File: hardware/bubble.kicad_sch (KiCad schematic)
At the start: 56 parts, among them J1 Barrel_Jack_Switch, Q1 AO3400A, U1 i7220, U2 i7230, U3 i7254, U4 i7250, U5 i7254, U6 i7242, U7 LM7805_TO220

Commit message: hardware: new board schematic
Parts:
- removed A1: Arduino_Nano_v3.x, Module:Arduino_Nano, symbol MCU_Module:Arduino_Nano_v3.x
- removed C1, C11, C13, C15, C16, C17, C2, C21, C3, C9: 100nF, Capacitor_SMD:C_0603_1608Metric, symbol Device:C_Small
- removed C10, C12, C14, C18, C22, C4, C5, C6, C7, C8: 22uF, Capacitor_SMD:C_1206_3216Metric, symbol Device:C_Small
- removed C19, C20: 120pF, Capacitor_SMD:C_0603_1608Metric, symbol Device:C_Small
- removed C23: 1uF, Capacitor_SMD:C_0603_1608Metric, symbol Device:C_Small
- removed C24: 2.2uF, Capacitor_SMD:C_0603_1608Metric, symbol Device:C_Small
- removed C25, C26: 1000uF, Capacitor_THT:CP_Radial_D8.0mm_P5.00mm, symbol Device:C_Polarized_Small_US
- removed J1: Barrel_Jack_Switch, Connector_BarrelJack:BarrelJack_GCT_DCJ200-10-A_Horizontal, symbol Connector:Barrel_Jack_Switch
- removed JP1, JP2: ~, Connector_PinSocket_2.54mm:PinSocket_1x02_P2.54mm_Vertical, symbol Jumper:Jumper_2_Bridged
- removed L1, L2, L3: .22uH, Inductor_SMD:L_1008_2520Metric, symbol Device:L_Small
- removed Q1: AO3400A, Package_TO_SOT_SMD:SOT-23, symbol Transistor_FET:AO3400A
- removed R1, R3, R5: 5.6k, Resistor_SMD:R_0603_1608Metric, symbol Device:R_Small
- removed R10, R11, R8, R9: 1k 2W, Resistor_SMD:R_2512_6332Metric, symbol Device:R_Small
- removed R12, R6: 5.1, Resistor_SMD:R_0805_2012Metric, symbol Device:R_Small
- removed R13: 33k, Resistor_SMD:R_0603_1608Metric, symbol Device:R_Small
- removed R14: 12k, Resistor_SMD:R_0603_1608Metric, symbol Device:R_Small
- removed R2: 3.48k 1%, Resistor_SMD:R_0603_1608Metric, symbol Device:R_Small
- removed R4: 47, Resistor_SMD:R_0805_2012Metric, symbol Device:R_Small
- removed R7: 10, Resistor_SMD:R_0603_1608Metric, symbol Device:R_Small
- removed U1: i7220, Package_DIP:DIP-40_W15.24mm, symbol intel_bubble:i7220
- removed U2: i7230, Package_DIP:DIP-22_W7.62mm, symbol intel_bubble:i7230
- removed U3, U5: i7254, Package_DIP:DIP-14_W7.62mm, symbol intel_bubble:i7254
- removed U4: i7250, Package_DIP:DIP-16_W7.62mm, symbol intel_bubble:i7250
- removed U6: i7242, Package_DIP:DIP-20_W7.62mm, symbol intel_bubble:i7242
- removed U7: LM7805_TO220, Package_TO_SOT_THT:TO-220-3_Vertical, symbol Regulator_Linear:LM7805_TO220
- added C1, C4: 0.33 uF, symbol Device:C
- added C10, C15: 15uF 20V 20%, symbol Device:C
- added C11, C12: 120pF 100V 5%, symbol Device:C
- added C13, C14, C8: 0.1uF, symbol Device:C
- added C2: 47 uF, symbol Device:C
- added C3, C5: 0.1 uF, symbol Device:C
- added C6: 120 uF, symbol Device:C
- added C7: 2.2 uF 20V 10%, symbol Device:C
- added C9: 15uF 20V 20%, symbol Device:C_Polarized
- added JP1: Only for reseed, Connector_PinHeader_2.54mm:PinHeader_1x02_P2.54mm_Vertical, symbol Jumper:Jumper_2_Open
- added L1, L2, L3: 0.22 uH, Inductor_SMD:L_0603_1608Metric_Pad1.05x0.95mm_HandSolder, symbol Device:L
- added Q1: BS170, Package_TO_SOT_THT:TO-92_Inline, symbol Transistor_FET:BS170
- added R1, R3: 33 kOhm, Resistor_SMD:R_0805_2012Metric_Pad1.20x1.40mm_HandSolder, symbol Device:R
- added R10, R11, R8, R9: 1kOhm, Resistor_SMD:R_0805_2012Metric_Pad1.20x1.40mm_HandSolder, symbol Device:R
- added R12, R7: 5.1 kOhm, Resistor_SMD:R_0805_2012Metric_Pad1.20x1.40mm_HandSolder, symbol Device:R
- added R13: 10Ohm, Resistor_SMD:R_0805_2012Metric_Pad1.20x1.40mm_HandSolder, symbol Device:R
- added R2: 3.48 kOhm, Resistor_SMD:R_0805_2012Metric_Pad1.20x1.40mm_HandSolder, symbol Device:R
- added R4, R5: 5.1 Ohm, Resistor_SMD:R_0805_2012Metric_Pad1.20x1.40mm_HandSolder, symbol Device:R
- added R6: 47 Ohm, Resistor_SMD:R_0805_2012Metric_Pad1.20x1.40mm_HandSolder, symbol Device:R
- added U1, U4: i7254, Package_DIP:DIP-14_W7.62mm, symbol intel_bubble:i7254
- added U2: i7250, Package_DIP:DIP-16_W7.62mm, symbol intel_bubble:i7250
- added U3: 74LS74, Package_DIP:DIP-14_W7.62mm, symbol 74xx:74LS74
- added U5: i7230, Package_DIP:DIP-22_W10.16mm, symbol intel_bubble:i7230
- added U6: i7220, Package_DIP:DIP-40_W15.24mm, symbol intel_bubble:i7220
- added U7: i7242, Package_DIP:DIP-20_W7.62mm, symbol intel_bubble:i7242
- added Y1: 8.000 MHz, Oscillator:Oscillator_DIP-8, symbol Oscillator:CXO_DIP8
- MBM1: footprint intel_bubble:MBM_dual -> intel_bubble:MBM_socket; LCSC Part # N/A -> (none)
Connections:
- net SWAP is gone; now on an unnamed net: MBM1.14 (SWAP.B)
- net +12V: now also JP1.2 (B), L1.1, R13.2, R4.2, R6.2, U1.13 (S4), U1.6 (S2), U4.13 (S4), U4.6 (S2)
- net +5V: now also C13.1, L2.1, R12.1, R3.2, R7.1, U3.1 (~{R}), U3.14 (VCC), U3.4 (~{S}), U7.20 (VCC), Y1.1 (EN), Y1.8 (Vcc)
- net A0: now also U6.10 (A0)
- net CLK: now also U3.5 (Q), U6.3 (CLK), U7.18 (CLK)
- net D0: now also U6.11 (D0)
- net D1: now also U6.12 (D1)
- net D2: now also U6.13 (D2)
- net D3: now also U6.14 (D3)
- net D4: now also U6.15 (D4)
- net D5: now also U6.16 (D5)
- net D6: now also U6.17 (D6)
- net D7: now also U6.18 (D7)
- net GND: now also C1.2, C13.2, C14.2, C15.2, C2.2, C3.2, C4.2, C5.2, C6.2, C7.1, Q1.3 (S), R5.1, U1.2 (S1), U1.9 (S3), U2.8 (GND), U3.7 (GND), U4.2 (S1), U4.9 (S3), U5.11 (GND), U5.12 (GND), U6.20 (GND), U7.1 (~{CS}), U7.10 (GND), Y1.4 (GND)
- net INT: now also U6.9 (INT)
- net ~{BUS.RD}: now also U6.25 (~{BUS.RD})
- net ~{DACK}: now also U6.7 (~{DACK})
- net ~{RD}: now also U6.5 (~{RD})
- net ~{WAIT}: now also R12.2, U6.26 (~{WAIT})
- net ~{WR}: now also U6.6 (~{WR})
- net at MBM1.1 (PULSE.COM(+12V)), MBM1.6 (PULSE.COM(+12V)): now also C10.2
- net at MBM1.17 (DET.OUT.B+): now also R9.1
- net at MBM1.18 (DET.OUT.A-): now also R10.1
- net at MBM1.20 (DET.SUPPLY): now also C8.1, C9.1, R4.1
- net at MBM1.15 (DET.COM): now also C8.2, C9.2, R5.2
- net at MBM1.13 (SWAP.A): now also U5.17 (SWAP)
- net at MBM1.16 (DET.OUT.B-): now also R8.1
- net at MBM1.19 (DET.OUT.A+): now also R11.1
- net BOOT.REP: no longer names the net of MBM1.4 (BOOT.REP)
- net BOOT.REP: now also U5.13 (BOOT.REP)
- net BOOT.SWAP: no longer names the net of MBM1.5 (BOOT.SWAP)
- net BOOT.SWAP: now also U5.14 (BOOT.SWAP)
- net GEN.A: no longer names the net of MBM1.7 (GEN.A)
- net GEN.A: now also U5.18 (GEN.A)
- net GEN.B: no longer names the net of MBM1.8 (GEN.B)
- net GEN.B: now also U5.19 (GEN.B)
- net REP.A: no longer names the net of MBM1.3 (REP.A)
- net REP.A: now also U5.15 (REP.A)
- net REP.B: no longer names the net of MBM1.2 (REP.B)
- net REP.B: now also U5.16 (REP.B)
- net X+.COIL: no longer names the net of MBM1.10 (X+.COIL.IN)
- net X+.COIL: now also U1.1 (D1), U1.14 (D4)
- net X-.COIL: no longer names the net of MBM1.9 (X-.COIL.IN)
- net X-.COIL: now also U1.7 (D2), U1.8 (D3)
- net Y+.COIL: no longer names the net of MBM1.12 (Y+.COIL.IN)
- net Y+.COIL: now also U4.1 (D1), U4.14 (D4)
- net Y-.COIL: no longer names the net of MBM1.11 (Y-.COIL.IN)
- net Y-.COIL: now also U4.7 (D2), U4.8 (D3)
- new net: C7.2, R1.1, R3.1, U5.21 (~{PWR.FAIL}), U6.1 (~{PWR.FAIL})
- new net: C11.1, R11.2, U7.6 (DET.A+)
- new net: C11.2, R10.2, U7.7 (DET.A-)
- new net: C4.1, L2.2, L3.1
- new net: U3.3 (C), Y1.5 (OUT)
- new net: C14.1, C15.1, R13.1, U7.5 (VDD)
- new net: U3.2 (D), U3.6 (~{Q})
- new net: Q1.1 (D), R2.1
- new net: R2.2, U5.20 (REFR)
- new net: U2.1 (~{CS}), U5.7 (~{CS}), U7.13 (~{ENABLE.A})
- new net: U2.10 (Y+.OUT), U4.10 (G3)
- new net: U2.11 (~{Y+.OUT}), U4.12 (G4)
- new net: U1.3 (G1), U2.12 (X-.OUT)
- new net: U1.5 (G2), U2.13 (~{X-.OUT})
- new net: U1.10 (G3), U2.14 (X+.OUT)
- new net: U1.12 (G4), U2.15 (~{X+.OUT})
- new net: Q1.2 (G), R1.2, U2.2 (~{RESET}), U6.2 (~{RESET.OUT}), U7.16 (~{RESET})
- new net: U2.3 (~{X+.IN}), U6.39 (~{X+})
- new net: U2.4 (~{X-.IN}), U6.38 (~{X-})
- new net: U2.5 (~{Y+.IN}), U6.37 (~{Y+})
- new net: U2.6 (~{Y-.IN}), U6.36 (~{Y-})
- new net: U2.7 (Y-.OUT), U4.3 (G1)
- new net: U2.9 (~{Y-.OUT}), U4.5 (G2)
- new net: C10.1, JP1.1 (A), R6.1
- new net: C12.1, R9.2, U7.8 (DET.B+)
- new net: C12.2, R8.2, U7.9 (DET.B-)
- new net: U5.10 (~{BOOT.EN}), U6.32 (~{BOOT.EN})
- new net: U5.2 (~{TM.A}), U6.35 (~{TM.A})
- new net: U5.3 (~{TM.B}), U6.34 (~{TM.B})
- new net: U5.4 (~{GEN.EN.B}), U7.12 (~{DATA.OUT.B})
- new net: U5.5 (~{GEN.EN.A}), U7.11 (~{DATA.OUT.A})
- new net: U5.6 (~{SWAP.EN}), U6.31 (~{SWAP.EN})
- new net: U5.8 (~{REP.EN}), U6.33 (~{REP.EN})
- new net: U5.9 (~{BOOT.SW.EN}), U6.30 (~{BOOT.SW.EN})
- new net: U6.22 (DIO), U7.17 (DIO)
- new net: U6.23 (~{SYNC}), U7.19 (~{SELECT.IN})
- new net: U6.24 (~{SHIFT.CLK}), U7.15 (~{SHIFT.CLK})
- new net: U6.29 (C/~{D}), U7.3 (C/~{D})
- new net D8: U6.19 (D8)
- new net DRQ: U6.8 (DRQ)
- new net VCC_MBM_CH: C5.1, C6.1, L3.2, U5.22 (VCC), U6.40 (VCC)
- new net VDD_MBM_CH: C1.1, C2.1, C3.1, L1.2, U2.16 (VDD), U5.1 (VDD)
- new net ~{CS}: U6.21 (~{CS})
- new net ~{DET.ON}: U6.28 (~{DET.ON})
- new net ~{ERR_FLAG}: R7.2, U6.27 (~{ERR.FLG}), U7.4 (~{ERR.FLG})
- new net ~{RESET}: U6.4 (~{RESET})
- no-connect marks 21 -> 8
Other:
- note removed: "JUMPER PROVIDED FOR 7110AZ - SHORT FOR NON-AZ"
- company: UNIX-HATERS Federation -> (none)
- title: UHF Bubble Def*cker -> Bubblator

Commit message: hardware: add more capacitors, fix critical mistakes in schematic
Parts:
- removed C1, C4: 0.33 uF, symbol Device:C
- removed C2: 47 uF, symbol Device:C
- removed C3, C5: 0.1 uF, symbol Device:C
- removed C6: 120 uF, symbol Device:C
- removed L1, L2, L3: 0.22 uH, Inductor_SMD:L_0603_1608Metric_Pad1.05x0.95mm_HandSolder, symbol Device:L
- removed R10, R11, R8, R9: 1kOhm, Resistor_SMD:R_0805_2012Metric_Pad1.20x1.40mm_HandSolder, symbol Device:R
- added C24, C30, C31: 0.1uF, Capacitor_SMD:C_0805_2012Metric_Pad1.18x1.45mm_HandSolder, symbol Device:C
- added C28, C3, C32, C5, C6: 47uF, Capacitor_THT:CP_Radial_D5.0mm_P2.00mm, symbol Device:C_Polarized
- added C29, C33, C4: 22uF, Capacitor_THT:CP_Radial_D5.0mm_P2.00mm, symbol Device:C_Polarized
- added RN1: 1k, Resistor_THT:R_Array_SIP8, symbol Device:R_Pack04
- C10, C9: value 15uF 20V 20% -> 22uF 25V; footprint (none) -> Capacitor_THT:CP_Radial_D5.0mm_P2.00mm
- C11, C12: value 120pF 100V 5% -> 120 pF 100V 5%; footprint (none) -> Capacitor_THT:C_Disc_D5.0mm_W2.5mm_P2.50mm
- C13, C14, C8: footprint (none) -> Capacitor_SMD:C_0805_2012Metric_Pad1.18x1.45mm_HandSolder
- C15: value 15uF 20V 20% -> 0.1uF; footprint (none) -> Capacitor_SMD:C_0805_2012Metric_Pad1.18x1.45mm_HandSolder
- C7: value 2.2 uF 20V 10% -> 2.2uF; footprint (none) -> Capacitor_THT:C_Radial_D4.0mm_H7.0mm_P1.50mm
- R1, R3: value 33 kOhm -> 33k
- R12, R7: value 5.1 kOhm -> 5.1k
- R13: value 10Ohm -> 10
- R2: value 3.48 kOhm -> 3.48k
- R4, R5: value 5.1 Ohm -> 5.1
- R6: value 47 Ohm -> 47
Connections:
- net VCC_MBM_CH is gone; now on net +5V: U5.22 (VCC), U6.40 (VCC)
- net VDD_MBM_CH is gone; now on net +12V: U2.16 (VDD), U5.1 (VDD)
- net +12V: now also C28.1, C29.1, C30.1, C31.1, C32.1, C33.1
- net +5V: now also C15.1, C24.1, C3.1, C5.1, C6.1
- net GND: now also C24.2, C28.2, C29.2, C3.2, C30.2, C31.2, C32.2, C33.2, C4.2, C5.2, C6.2
- net at C11.1, U7.6 (DET.A+): now also RN1.4 (R4.1)
- net at C11.2, U7.7 (DET.A-): now also RN1.3 (R3.1)
- net at C14.1, R13.1, U7.5 (VDD): now also C4.1; no longer C15.1
- net at C12.1, U7.8 (DET.B+): now also RN1.2 (R2.1)
- net at C12.2, U7.9 (DET.B-): now also RN1.1 (R1.1)
- net at MBM1.18 (DET.OUT.A-): now also RN1.6 (R3.2)
- net at MBM1.19 (DET.OUT.A+): now also RN1.5 (R4.2)
- net at MBM1.16 (DET.OUT.B-): now also RN1.8 (R1.2)
- net at MBM1.17 (DET.OUT.B+): now also RN1.7 (R2.2)
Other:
- note added: "Clock generator"
- note added: "Pull-up resistors"
- moved on the sheet: C10, C11, C12, C13, C14, C7, C8, C9, JP1, MBM1, Q1, R1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

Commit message: hardware: minor cleanup
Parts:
- removed C7: 2.2uF, Capacitor_THT:C_Radial_D4.0mm_H7.0mm_P1.50mm, symbol Device:C
- added C34, C35: 2.2uF, Capacitor_THT:CP_Radial_D5.0mm_P2.00mm, symbol Device:C_Polarized
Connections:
- net GND: now also C34.2, C35.2
- net at R1.1, R3.1, U5.21 (~{PWR.FAIL})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: now also C34.1
- net at Q1.2 (G), R1.2, U2.2 (~{RESET})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: now also C35.1
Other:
- note added: "TODO: Verify this with Compass"
- moved on the sheet: C10, C11, C12, C13, C14, C15, C24, C28, C29, C3, C30, C31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

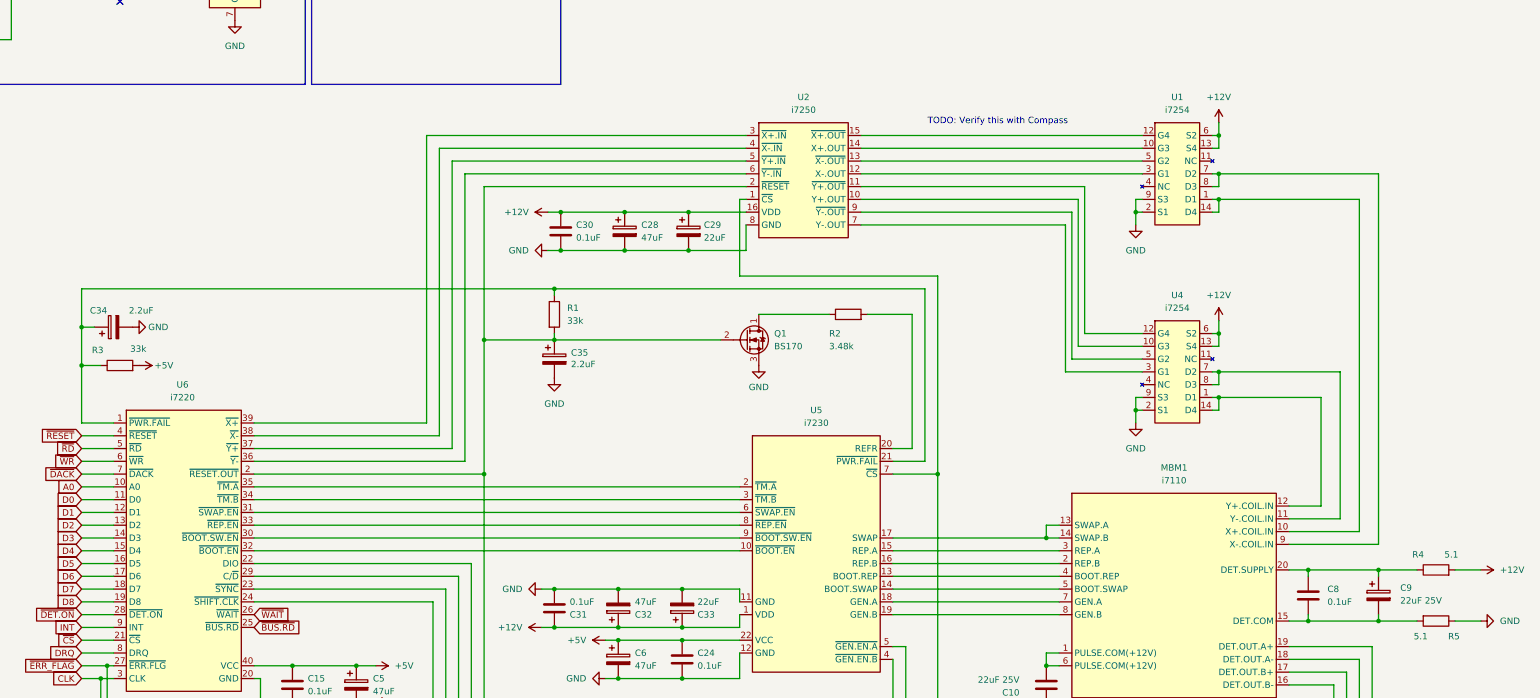
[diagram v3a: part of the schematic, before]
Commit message: hardware: add capacitors near i7254
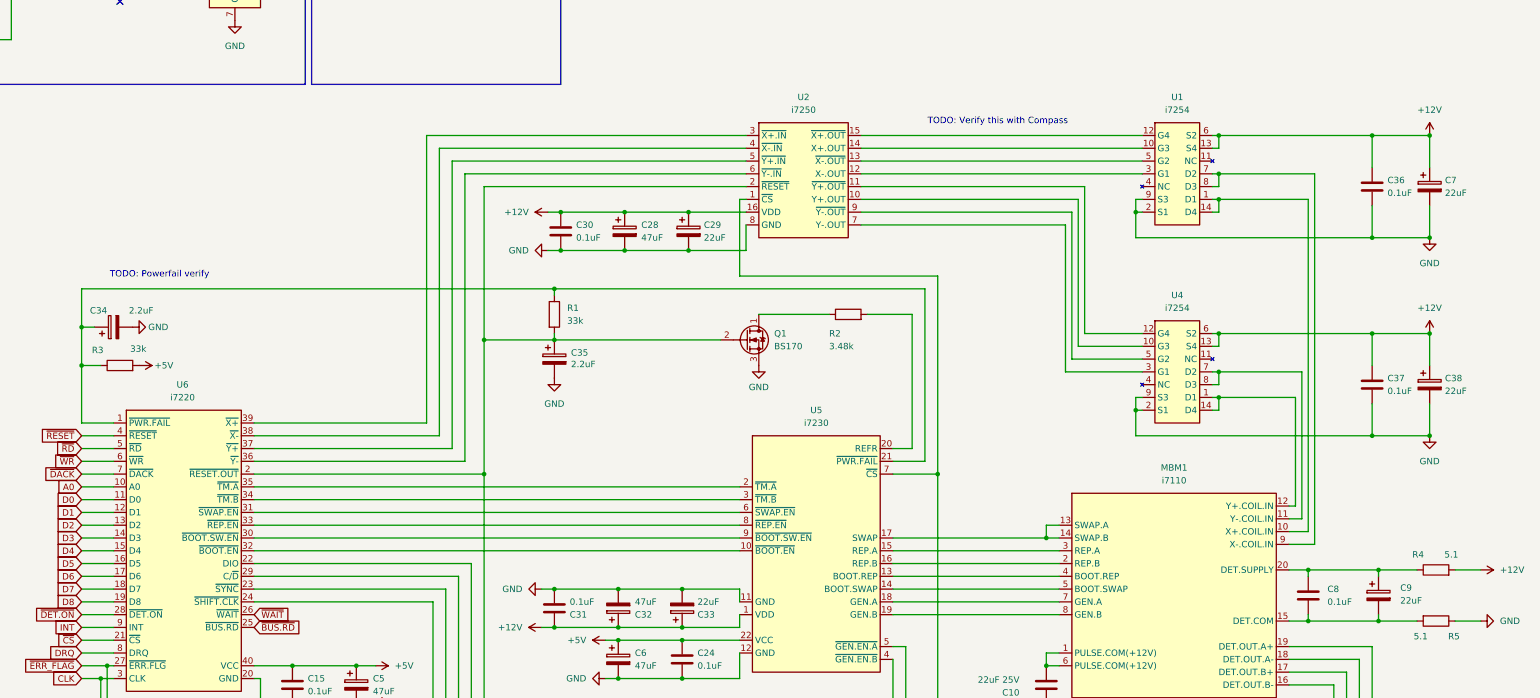
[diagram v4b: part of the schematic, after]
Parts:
- added C36, C37: 0.1uF, Capacitor_SMD:C_0805_2012Metric_Pad1.18x1.45mm_HandSolder, symbol Device:C
- added C38, C7: 22uF, Capacitor_THT:CP_Radial_D5.0mm_P2.00mm, symbol Device:C_Polarized
- C9: value 22uF 25V -> 22uF
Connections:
- net +12V: now also C36.1, C37.1, C38.1, C7.1
- net GND: now also C36.2, C37.2, C38.2, C7.2
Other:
- note added: "TODO: Powerfail verify"

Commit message: hardware: connect MBM module like Compass
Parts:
- removed C34, C35: 2.2uF, Capacitor_THT:CP_Radial_D5.0mm_P2.00mm, symbol Device:C_Polarized
- removed R1, R3: 33k, Resistor_SMD:R_0805_2012Metric_Pad1.20x1.40mm_HandSolder, symbol Device:R
- U3: footprint Package_DIP:DIP-14_W7.62mm -> Package_SO:SOIC-14_3.9x8.7mm_P1.27mm
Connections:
- net ~{7220 POWER.FAIL}: now reaches U6.1 (~{PWR.FAIL})
- net ~{7220 POWER.FAIL}: no longer U5.21 (~{PWR.FAIL})
- net at U2.12 (X-.OUT): now also U1.10 (G3); no longer U1.3 (G1)
- net at U2.13 (~{X-.OUT}): now also U1.12 (G4); no longer U1.5 (G2)
- net at U2.14 (X+.OUT): now also U1.3 (G1); no longer U1.10 (G3)
- net at U2.15 (~{X+.OUT}): now also U1.5 (G2); no longer U1.12 (G4)
- net ~{RESET.BUS}: now reaches Q1.2 (G), U2.2 (~{RESET}), U7.16 (~{RESET})
- net ~{RESET.BUS}: no longer U6.2 (~{RESET.OUT})
- net at U1.1 (D1), U1.14 (D4): now also MBM1.9 (X-.COIL.IN); no longer MBM1.10 (X+.COIL.IN)
- net at U1.7 (D2), U1.8 (D3): now also MBM1.10 (X+.COIL.IN); no longer MBM1.9 (X-.COIL.IN)
- net ~{RESET} renamed ~{7220 RESET.IN}
- new net ~{7220 RESET.OUT}: U6.2 (~{RESET.OUT})
- new net ~{POWER.FAIL}: U5.21 (~{PWR.FAIL})
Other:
- note added: "Reset and power fail"
- note added: "This wiring is taken from GRiD Compass, not from Intel docs"
- note removed: "TODO: Powerfail verify"
- note removed: "TODO: Verify this with Compass"
- moved on the sheet: C10, C11, C12, C13, C14, C15, C24, C28, C29, C3, C30, C31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

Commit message: hardware: add powerfail circuit, rework power
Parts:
- removed C24, C31: 0.1uF, Capacitor_SMD:C_0805_2012Metric_Pad1.18x1.45mm_HandSolder, symbol Device:C
- removed C32, C6: 47uF, Capacitor_THT:CP_Radial_D5.0mm_P2.00mm, symbol Device:C_Polarized
- removed C33: 22uF, Capacitor_THT:CP_Radial_D5.0mm_P2.00mm, symbol Device:C_Polarized
- added C1: 0.33 uF, Capacitor_THT:C_Rect_L13.0mm_W6.5mm_P7.50mm_P10.00mm, symbol Device:C
- added C2: 22uF, Capacitor_THT:CP_Radial_D4.0mm_P1.50mm, symbol Device:C_Polarized
- added C23: 2.2 uF, Capacitor_SMD:C_0805_2012Metric_Pad1.18x1.45mm_HandSolder, symbol Device:C
- added C26, C27: 0.01 uF, Capacitor_SMD:C_0805_2012Metric_Pad1.18x1.45mm_HandSolder, symbol Device:C
- added C28: 10 uF, Capacitor_SMD:C_0805_2012Metric_Pad1.18x1.45mm_HandSolder, symbol Device:C
- added C3: 47uF, Capacitor_THT:CP_Radial_D5.0mm_P2.00mm, symbol Device:C_Polarized
- added C4: 150uF, Capacitor_THT:CP_Radial_D10.0mm_P2.50mm, symbol Device:C_Polarized
- added C6, C7: 0.1uF, Capacitor_SMD:C_0805_2012Metric_Pad1.18x1.45mm_HandSolder, symbol Device:C
- added D1: POWER FAILED LED, LED_SMD:LED_0805_2012Metric_Pad1.15x1.40mm_HandSolder, symbol Device:LED
- added D2, D3: D, Diode_SMD:D_SOD-323_HandSoldering, symbol Device:D
- added L1, L2, L3: 0.22 uH, Inductor_SMD:L_APV_APH0530, symbol Device:L
- added Q2: DTC113Z, Package_TO_SOT_SMD:SOT-23-3, symbol Transistor_BJT:DTC113Z
- added R10: 33k, Resistor_SMD:R_0805_2012Metric_Pad1.20x1.40mm_HandSolder, symbol Device:R
- added R13: 5.1k, Resistor_SMD:R_0805_2012Metric_Pad1.20x1.40mm_HandSolder, symbol Device:R
- added R5: 300, Resistor_SMD:R_0805_2012Metric_Pad1.20x1.40mm_HandSolder, symbol Device:R
- added R7: 1k, Resistor_SMD:R_0805_2012Metric_Pad1.20x1.40mm_HandSolder, symbol Device:R
- added R8: 3.9k, Resistor_SMD:R_0805_2012Metric_Pad1.20x1.40mm_HandSolder, symbol Device:R
- added R9: 5.5k, Resistor_SMD:R_0805_2012Metric_Pad1.20x1.40mm_HandSolder, symbol Device:R
- added U6: 74AHC1G00, Package_TO_SOT_SMD:SOT-23-5_HandSoldering, symbol 74xGxx:74AHC1G00
- added U9: 74LVC1G07, Package_TO_SOT_SMD:SOT-23-5_HandSoldering, symbol 74xGxx:74LVC1G07
- renumbered C28 to C10, C3 to C11, C29 to C12, C4 to C15, C10 to C16, C11 to C17, C12 to C18, C8 to C19, C36 to C20, C37 to C21, C9 to C22, C7 to C24, C38 to C25, C15 to C5, C5 to C8, C30 to C9, R7 to R1, R4 to R11, R5 to R12, R12 to R2, R2 to R3, R13 to R4, U3 to U1, U6 to U2, U7 to U3, U2 to U4, U1 to U7, U4 to U8
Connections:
- net ~{7220 RESET.IN} is gone; now on net ~{POWER.FAIL}: U2.4 (~{RESET})
- net +12V: now also L2.2; no longer U5.1 (VDD)
- net +5V: now also D1.2 (A), L1.2, R13.2, R7.1, U6.5 (VCC), U9.5 (VCC); no longer U5.22 (VCC)
- net GND: now also C1.2, C2.2, C23.2, C26.2, C27.2, C28.2, C3.2, C4.2, C6.2, C7.2, Q2.2 (E), R10.2, U6.3 (GND), U9.3 (GND)
- net ~{7220 POWER.FAIL}: now also C23.1, C26.1, D3.2 (A), Q2.3 (C), R8.2
- net ~{7220 RESET.OUT}: now also R13.1, U6.2, U9.2
- net ~{POWER.FAIL}: now also C27.1, D2.2 (A), R5.1, R7.2, U6.1
- net ~{RESET.BUS}: now also C28.1, R10.1, R9.2, U9.4
- new net: D2.1 (K), R8.1
- new net: D1.1 (K), R5.2
- new net: D3.1 (K), R9.1
- new net: C1.1, L1.1, L3.2
- new net: Q2.1 (B), U6.4
- new net 7230 VCC: C4.1, C7.1, L3.1, U5.22 (VCC)
- new net 7230 VDD: C2.1, C3.1, C6.1, L2.1, U5.1 (VDD)
- no-connect marks 8 -> 9
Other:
- note added: "AP-187. Page 17. Figure 13: Powerfail circuit rev. 2 75463 was replaced with a few transistors and gates"
- note added: "AP-187. Page 18. Figure 14: Power Line Filter"
- note added: "Reset and powerfail circuit"
- note removed: "Reset and power fail"
- moved on the sheet: C10, C11, C12, C13, C14, C15, C16, C17, C18, C19, C20, C21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
